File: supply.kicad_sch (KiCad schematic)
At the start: 57 parts, among them Q1 DMG1012T-7, Q3 DMG1012T-7, U1 AP62301_TSOT, U2 AP62301_TSOT, U3 NCP163ASN330T1G, U4 REF3012AIDBZT, U5 TLV73312PDBVT

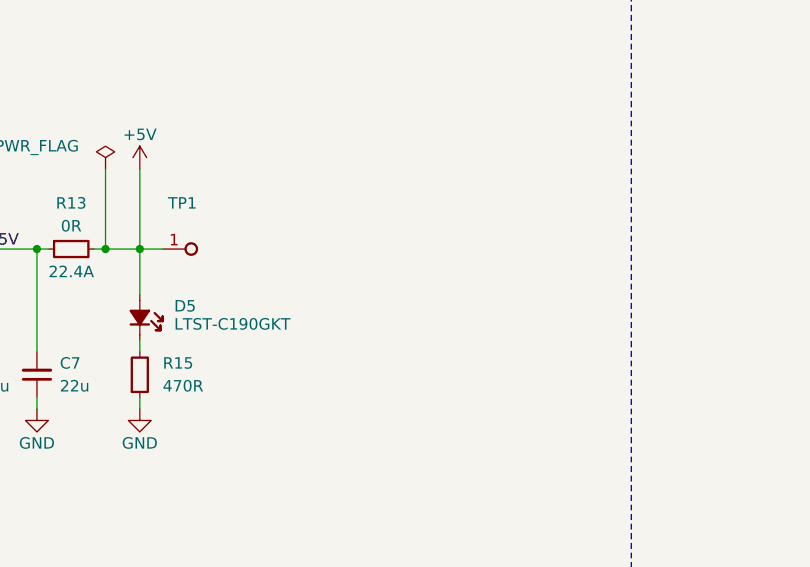
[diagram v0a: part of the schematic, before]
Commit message: [#55438] Add GND testpoint
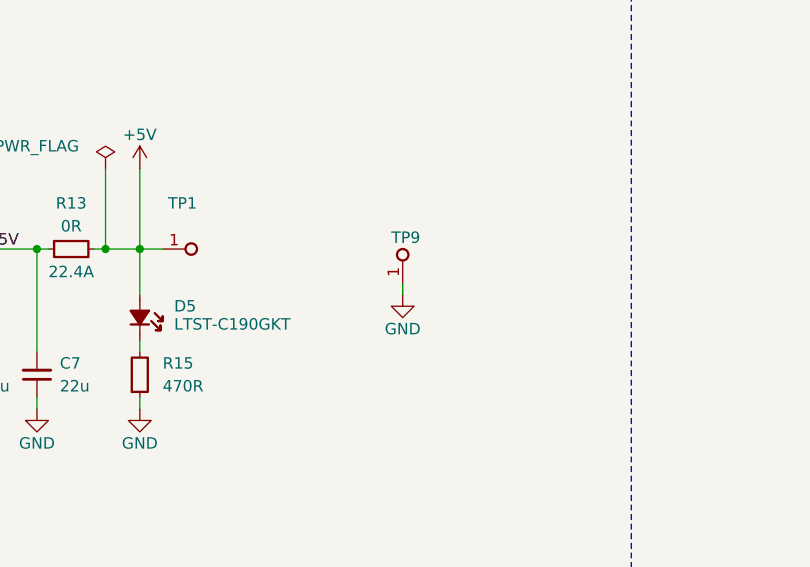
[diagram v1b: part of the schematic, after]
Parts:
- added TP9: TP_1.5mm_SMD, antmicro-footprints:TP_SMD_1.5mm, symbol antmicroTestPoints:TP_1.5mm_SMD
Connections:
- net GND: now also TP9.1
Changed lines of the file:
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@@
     (stroke (width 0) (type default))
   )
+  (wire (pts (xy 195.58 127) (xy 195.58 125.73))
+    (stroke (width 0) (type default))
+  )
   (wire (pts (xy 55.88 119.38) (xy 55.88 121.92))
     (stroke (width 0) (type default))
@@
     )
   )
+  (symbol (lib_id "antmicroTestPoints:TP_1.5mm_SMD") (at 195.58 125.73 90) (unit 1)
+    (in_bom yes) (on_board yes) (dnp no)
+    (property "Reference" "TP9" (at 194.31 120.65 90)
+      (effects (font (size 1.27 1.27) (thickness 0.15)) (justify right))
+    )
+    (property "Value" "TP_1.5mm_SMD" (at 203.2 110.49 0)
+      (effects (font (size 1.27 1.27) (thickness 0.15)) (justify left bottom) hide)
+    )
+    (property "Footprint" "antmicro-footprints:TP_SMD_1.5mm" (at 205.74 110.49 0)
+      (effects (font (size 1.27 1.27) (thickness 0.15)) (justify left bottom) hide)
+    )
+    (property "Datasheet" "" (at 208.28 107.95 0)
+      (effects (font (size 1.27 1.27) (thickness 0.15)) (justify left bottom) hide)
+    )
+    (property "MPN" "" (at 195.58 125.73 0)
+      (effects (font (size 1.27 1.27)) hide)
+    )
+    (property "Manufacturer" "" (at 195.58 125.73 0)
+      (effects (font (size 1.27 1.27)) hide)
+    )
+    (property "Author" "Antmicro" (at 210.82 110.49 0)
+      (effects (font (size 1.27 1.27) (thickness 0.15)) (justify left bottom) hide)
+    )
+    (property "License" "Apache-2.0" (at 213.36 110.49 0)
+      (effects (font (size 1.27 1.27) (thickness 0.15)) (justify left bottom) hide)
+    )
+    (pin "1")
+    (instances
+      (project "gmsl-serializer"
+        (path "/dbd1044a-3803-4c19-8db2-96636cba7198/a0eea618-ebab-4bb8-b0df-45f61b300adb"
+          (reference "TP9") (unit 1)
+        )
+      )
+    )
+  )
   (symbol (lib_id "antmicropower:+5V") (at 351.79 106.68 0) (unit 1)
     (in_bom yes) (on_board yes) (dnp no)
@@
         )
       )
+    )
+  )
+  (symbol (lib_id "antmicropower:GND") (at 195.58 127 0) (unit 1)
+    (in_bom yes) (on_board yes) (dnp no)
+    (property "Reference" "#PWR015" (at 204.47 129.54 0)
+      (effects (font (size 1.27 1.27) (thickness 0.15)) (justify left bottom) hide)
+    )
+    (property "Value" "GND" (at 195.58 130.81 0)
+      (effects (font (size 1.27 1.27) (thickness 0.15)))
+    )
+    (property "Footprint" "" (at 204.47 134.62 0)
+      (effects (font (size 1.27 1.27) (thickness 0.15)) (justify left bottom) hide)
+    )
+    (property "Datasheet" "" (at 204.47 139.7 0)
+      (effects (font (size 1.27 1.27) (thickness 0.15)) (justify left bottom) hide)
+    )
+    (property "Author" "Antmicro" (at 204.47 134.62 0)
+      (effects (font (size 1.27 1.27) (thickness 0.15)) (justify left bottom) hide)
+    )
+    (property "License" "Apache-2.0" (at 204.47 137.16 0)
+      (effects (font (size 1.27 1.27) (thickness 0.15)) (justify left bottom) hide)
+    )
+    (pin "1")
+    (instances
+      (project "gmsl-serializer"
+        (path "/dbd1044a-3803-4c19-8db2-96636cba7198/a0eea618-ebab-4bb8-b0df-45f61b300adb"
+          (reference "#PWR015") (unit 1)
+        )
+      )

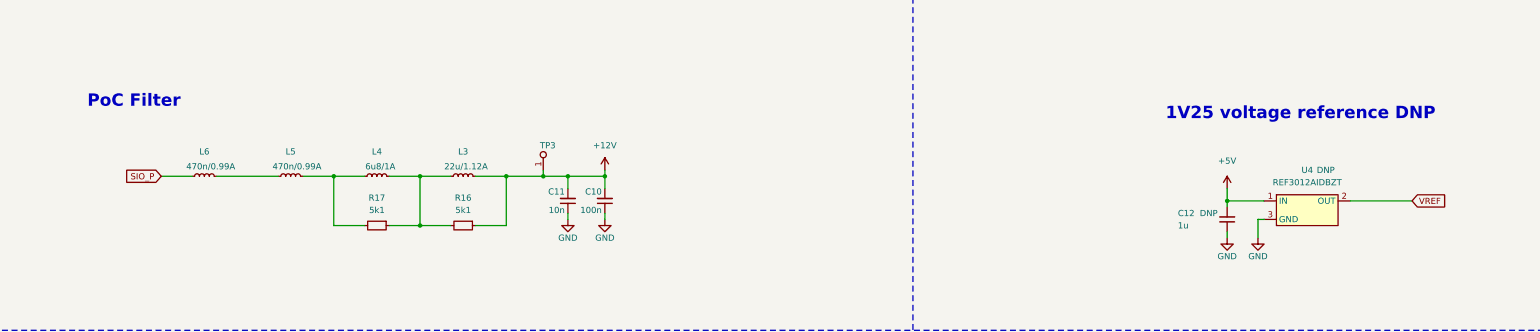
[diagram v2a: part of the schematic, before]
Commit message: [#66847] Make schematic hierarchical
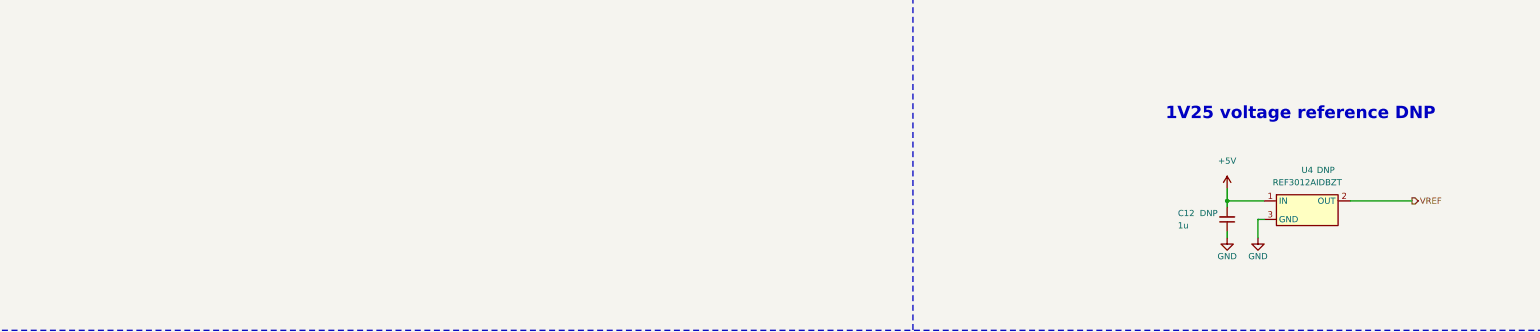
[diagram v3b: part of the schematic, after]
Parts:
- removed C10: C_100n_0402, antmicro-footprints:C_0402_1005Metric, symbol antmicroCapacitors0402:C_100n_0402
- removed C11: C_10n_0402, antmicro-footprints:C_0402_1005Metric, symbol antmicroCapacitors0402:C_10n_0402
- removed L3: L_22u_1.12A_Coilcraft-MSS6132T, antmicro-footprints:L_Coilcraft-MSS6132T, symbol antmicroFixedInductors:L_22u_1.12A_Coilcraft-MSS6132T
- removed L4: L_6u8_1A_Coilcraft-1210POC, antmicro-footprints:L_Coilcraft-1210POC, symbol antmicroFixedInductors:L_6u8_1A_Coilcraft-1210POC
- removed L5, L6: L_470n_1A_Coilcraft-PFL1609, antmicro-footprints:L_Coilcraft-PFL1609, symbol antmicroFixedInductors:L_470n_1A_Coilcraft-PFL1609
- removed R16, R17: R_5k1_0402, antmicro-footprints:R_0402_1005Metric, symbol antmicroResistors0402:R_5k1_0402
- removed TP3: TP_1.5mm_SMD, antmicro-footprints:TP_SMD_1.5mm, symbol antmicroTestPoints:TP_1.5mm_SMD
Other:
- note removed: "PoC Filter"

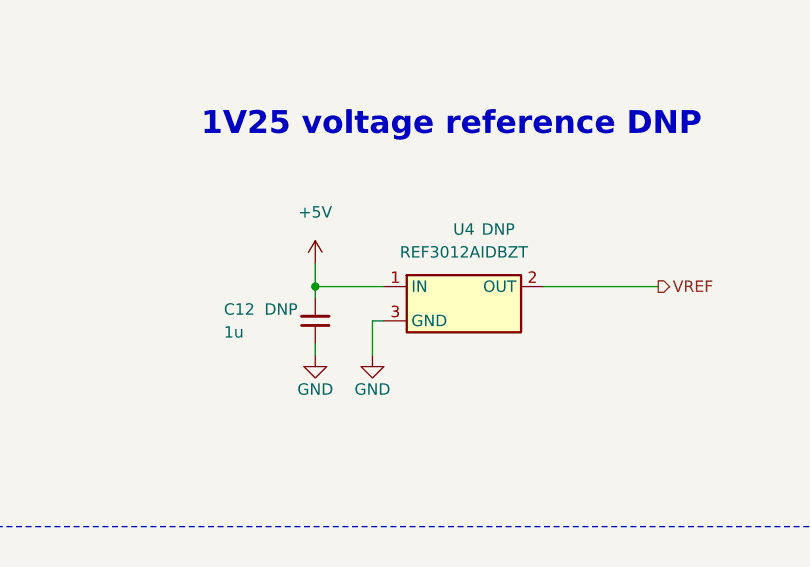
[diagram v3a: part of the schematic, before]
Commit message: [#66847] Update DNP style; Update from lib; Fix CSI bus definition
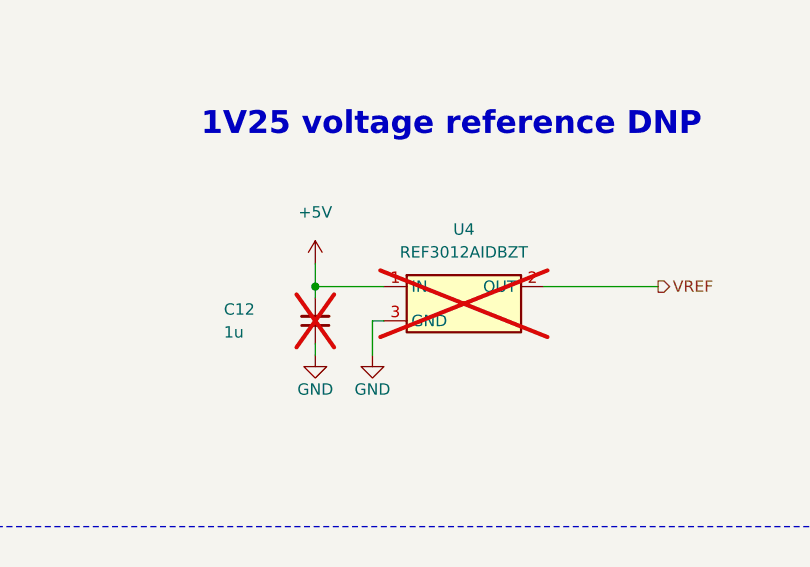
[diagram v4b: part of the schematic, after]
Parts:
- C12, U4: DNP DNP -> (none); now not fitted
- TP1, TP2, TP4, TP5, TP9: now left out of the parts list
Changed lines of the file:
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@@
   )
   (symbol (lib_id "antmicroTestPoints:TP_1.5mm_SMD") (at 156.21 217.17 0) (unit 1)
-    (in_bom yes) (on_board yes) (dnp no)
+    (in_bom no) (on_board yes) (dnp no)
     (property "Reference" "TP2" (at 161.29 214.63 0)
       (effects (font (size 1.27 1.27) (thickness 0.15)) (justify right))
@@
   )
   (symbol (lib_id "antmicroPMICPowerDistributionSwitchesLoadDrivers:REF3012AIDBZT") (at 293.37 54.61 0) (unit 1)
-    (in_bom yes) (on_board yes) (dnp no)
+    (in_bom yes) (on_board yes) (dnp yes)
     (property "Reference" "U4" (at 302.26 48.26 0)
       (effects (font (size 1.27 1.27) (thickness 0.15)))
@@
       (effects (font (size 1.27 1.27) (thickness 0.15)) (justify left bottom) hide)
     )
-    (property "DNP" "DNP" (at 306.07 48.26 0)
-      (effects (font (size 1.27 1.27)))
-    )
     (pin "1")
     (pin "2")
@@
   )
   (symbol (lib_id "antmicroCapacitors0402:C_1u_16V_0402") (at 285.75 60.96 90) (unit 1)
-    (in_bom yes) (on_board yes) (dnp no)
+    (in_bom yes) (on_board yes) (dnp yes)
     (property "Reference" "C12" (at 275.59 57.15 90)
       (effects (font (size 1.27 1.27) (thickness 0.15)) (justify right))
@@
     (property "Dielectric" "" (at 316.23 40.64 0)
       (effects (font (size 1.27 1.27)) (justify left bottom) hide)
-    )
-    (property "DNP" "DNP" (at 281.94 57.15 90)
-      (effects (font (size 1.27 1.27)))
     )
     (pin "1")
@@
   )
   (symbol (lib_id "antmicroTestPoints:TP_1.5mm_SMD") (at 168.91 121.92 0) (unit 1)
-    (in_bom yes) (on_board yes) (dnp no)
+    (in_bom no) (on_board yes) (dnp no)
     (property "Reference" "TP1" (at 172.72 116.84 0)
       (effects (font (size 1.27 1.27) (thickness 0.15)) (justify right))
@@
   )
   (symbol (lib_id "antmicroTestPoints:TP_1.5mm_SMD") (at 304.8 125.73 90) (unit 1)
-    (in_bom yes) (on_board yes) (dnp no)
+    (in_bom no) (on_board yes) (dnp no)
     (property "Reference" "TP5" (at 303.53 120.65 90)
       (effects (font (size 1.27 1.27) (thickness 0.15)) (justify right))
@@
   )
   (symbol (lib_id "antmicroTestPoints:TP_1.5mm_SMD") (at 195.58 125.73 90) (unit 1)
-    (in_bom yes) (on_board yes) (dnp no)
+    (in_bom no) (on_board yes) (dnp no)
     (property "Reference" "TP9" (at 194.31 120.65 90)
       (effects (font (size 1.27 1.27) (thickness 0.15)) (justify right))
@@
   )
   (symbol (lib_id "antmicroTestPoints:TP_1.5mm_SMD") (at 321.31 209.55 90) (unit 1)
-    (in_bom yes) (on_board yes) (dnp no)
+    (in_bom no) (on_board yes) (dnp no)
     (property "Reference" "TP4" (at 320.04 204.47 90)
       (effects (font (size 1.27 1.27) (thickness 0.15)) (justify right))

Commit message: [#66847] Change 3V3 LDO; Update L3 footprint
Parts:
- U3: value NCP163ASN330T1G -> AP7366-33W5-7; symbol antmicroPMICVoltageRegulatorsLinear:NCP163ASN330T1G -> antmicroPMICVoltageRegulatorsLinear:AP7366-33W5-7; MPN NCP163ASN330T1G -> AP7366-33W5-7; Manufacturer ON Semiconductor -> Diodes Incorporated
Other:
- moved on the sheet: C1, C2, C3, C4, C5, C6, C7, C8, D5, D8, D9, L1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
